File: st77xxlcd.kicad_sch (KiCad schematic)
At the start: 6 parts, among them J1 Conn_01x40_MountingPin, J2 Conn_01x06_MountingPin, J3 Conn_01x24_MountingPin, J4 Conn_02x20_Counter_Clockwise, J5 Conn_01x06_Pin, J6 Conn_01x24_Pin

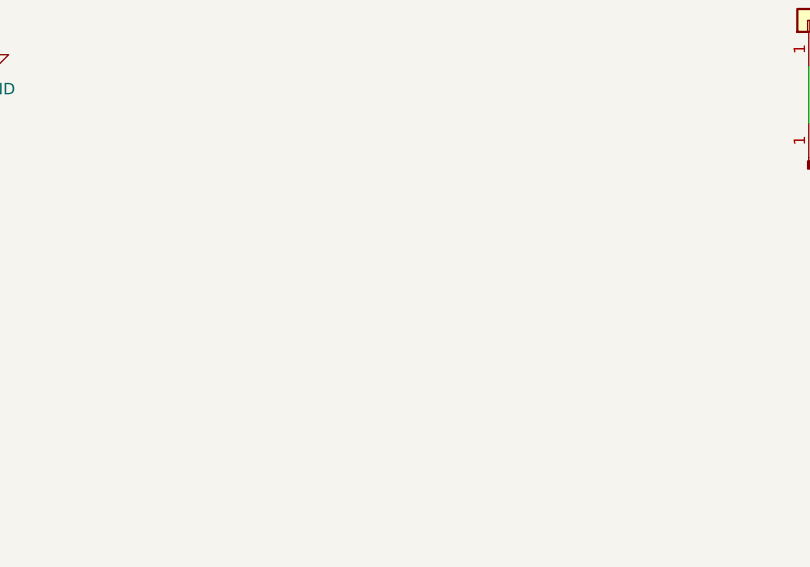
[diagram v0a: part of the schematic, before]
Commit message: [IMP] 完成布线，导出制造文件
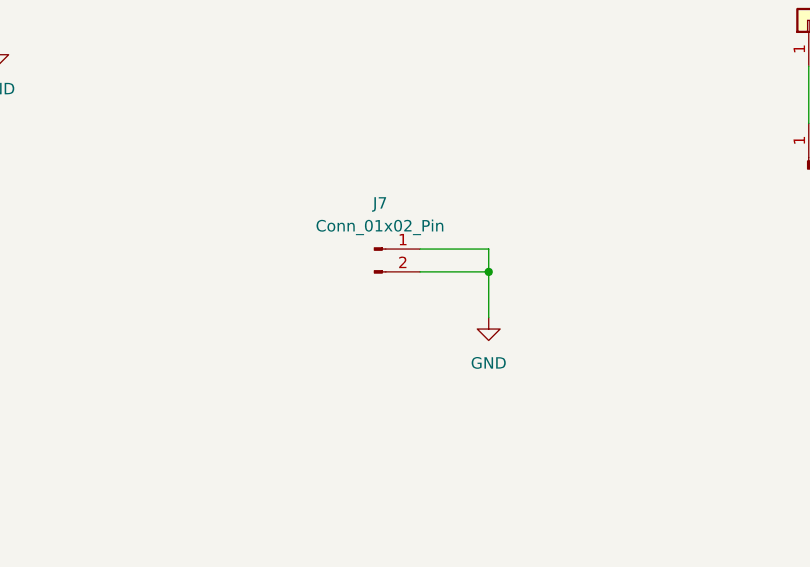
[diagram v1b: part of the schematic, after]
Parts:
- added J7: Conn_01x02_Pin, Connector_PinHeader_2.54mm:PinHeader_1x02_P2.54mm_Vertical, symbol Connector:Conn_01x02_Pin
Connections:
- net GND: now also J7.1 (Pin_1), J7.2 (Pin_2)
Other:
- title: (none) -> 显示屏调试接口板
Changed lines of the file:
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@@
 	(generator_version "9.0")
 	(paper "A3")
+	(title_block
+		(title "显示屏调试接口板")
+		(date "2025-03-28")
+		(rev "V1.0.0")
+	)
 	(text "4-SPI/8080 8bit"
 		(exclude_from_sim no)
@@
 		)
 	)
+	(junction
+		(at 265.43 50.8)
+		(diameter 0)
+		(color 0 0 0 0)
+	)
 	(wire
 		(pts
@@
 	(wire
 		(pts
+			(xy 265.43 50.8) (xy 265.43 55.88)
+		)
+		(stroke
+			(width 0)
+			(type default)
+		)
+	)
+	(wire
+		(pts
 			(xy 57.15 26.67) (xy 57.15 45.72)
 		)
@@
 	(wire
 		(pts
+			(xy 257.81 48.26) (xy 265.43 48.26)
+		)
+		(stroke
+			(width 0)
+			(type default)
+		)
+	)
+	(wire
+		(pts
 			(xy 19.05 26.67) (xy 19.05 45.72)
 		)
@@
 	(wire
 		(pts
+			(xy 265.43 48.26) (xy 265.43 50.8)
+		)
+		(stroke
+			(width 0)
+			(type default)
+		)
+	)
+	(wire
+		(pts
 			(xy 190.5 27.94) (xy 190.5 33.02)
 		)
@@
 	(wire
 		(pts
+			(xy 257.81 50.8) (xy 265.43 50.8)
+		)
+		(stroke
+			(width 0)
+			(type default)
+		)
+	)
+	(wire
+		(pts
 			(xy 200.66 27.94) (xy 200.66 33.02)
 		)
@@
 	)
 	(symbol
+		(lib_id "Connector:Conn_01x02_Pin")
+		(at 252.73 48.26 0)
+		(unit 1)
+		(exclude_from_sim no)
+		(in_bom yes)
+		(on_board yes)
+		(dnp no)
+		(fields_autoplaced yes)
+		(property "Reference" "J7"
+			(at 253.365 43.18 0)
+			(effects
+				(font
+					(size 1.27 1.27)
+				)
+			)
+		)
+		(property "Value" "Conn_01x02_Pin"
+			(at 253.365 45.72 0)
+			(effects
+				(font
+					(size 1.27 1.27)
+				)
+			)
+		)
+		(property "Footprint" "Connector_PinHeader_2.54mm:PinHeader_1x02_P2.54mm_Vertical"
+			(at 252.73 48.26 0)
+			(effects
+				(font
+					(size 1.27 1.27)
+				)
+				(hide yes)
+			)
+		)
+		(property "Datasheet" "~"
+			(at 252.73 48.26 0)
+			(effects
+				(font
+					(size 1.27 1.27)
+				)
+				(hide yes)
+			)
+		)
+		(property "Description" "Generic connector, single row, 01x02, script generated"
+			(at 252.73 48.26 0)
+			(effects
+				(font
+					(size 1.27 1.27)
+				)
+				(hide yes)
+			)
+		)
+		(pin "1"
+		)
+		(pin "2"
+		)
+		(instances
+			(project ""
+				(path "/c69a49e5-3c49-4e29-b181-1137224791f9"
+					(reference "J7")
+					(unit 1)
+				)
+			)
+		)
+	)
+	(symbol
 		(lib_id "Connector_Generic_MountingPin:Conn_01x40_MountingPin")
 		(at 64.77 21.59 90)
@@
 					(unit 1)
 				)
+			)
+		)
+	)
+	(symbol
+		(lib_id "power:GND")
+		(at 265.43 55.88 0)
+		(unit 1)
+		(exclude_from_sim no)
+		(in_bom yes)
+		(on_board yes)
+		(dnp no)
+		(fields_autoplaced yes)
+		(property "Reference" "#PWR04"
+			(at 265.43 62.23 0)
+			(effects
+				(font
+					(size 1.27 1.27)
+				)
+				(hide yes)
+			)
+		)
+		(property "Value" "GND"
+			(at 265.43 60.96 0)
+			(effects
+				(font
+					(size 1.27 1.27)
+				)
+			)
+		)
+		(property "Footprint" ""
+			(at 265.43 55.88 0)
+			(effects
+				(font
+					(size 1.27 1.27)
+				)
+				(hide yes)
+			)
+		)
+		(property "Datasheet" ""
+			(at 265.43 55.88 0)
+			(effects
+				(font
+					(size 1.27 1.27)
+				)
+				(hide yes)
+			)
+		)
+		(property "Description" "Power symbol creates a global label with name \"GND\" , ground"
+			(at 265.43 55.88 0)
+			(effects
+				(font
+					(size 1.27 1.27)
+				)
+				(hide yes)
+			)
+		)
+		(pin "1"
+		)
+		(instances
+			(project ""
+				(path "/c69a49e5-3c49-4e29-b181-1137224791f9"
+					(reference "#PWR04")
+					(unit 1)
+				)
